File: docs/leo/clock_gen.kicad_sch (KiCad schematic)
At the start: 6 parts, among them IC53 74LS74, IC54 7404, X2 26.6666Mhz

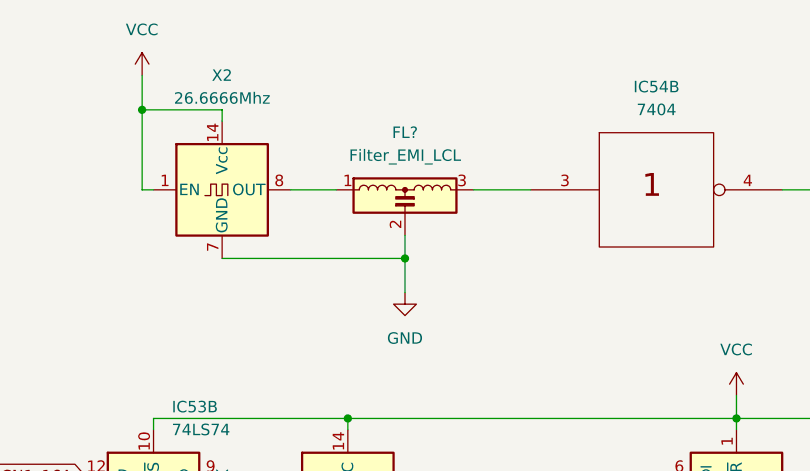
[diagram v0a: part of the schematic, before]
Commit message: Add ym filters and misinx path Upgrade to kicad 7
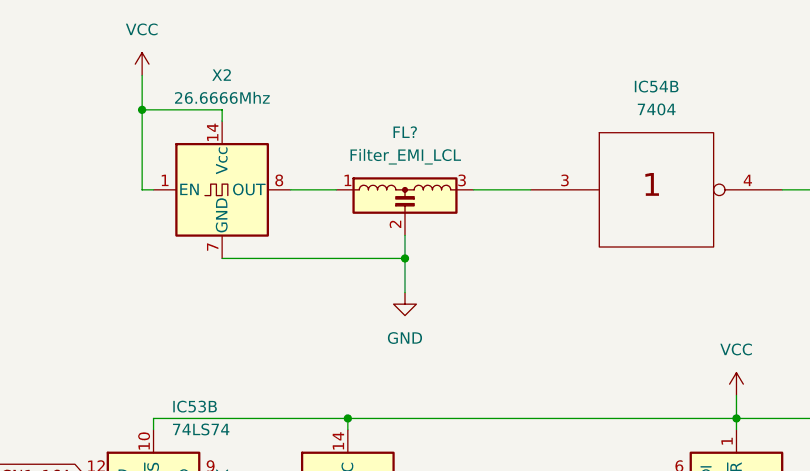
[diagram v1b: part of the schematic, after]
